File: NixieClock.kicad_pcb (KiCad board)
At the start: 2 copper layers, 164 parts, among them J1 Barrel_Jack, Q1 MPSA42, Q10 MPSA42, Q11 MPSA42, Q12 MPSA42, Q13 KSP92BU, Q14 KSP92BU, Q15 MPSA42, Q16 MPSA42, Q17 MPSA42, Q18 MPSA42, Q19 KSP92BU, Q2 MPSA42, Q20 KSP92BU, Q21 MPSA42, Q22 MPSA42, Q23 KSP92BU, Q24 KSP92BU, Q25 KSP2907A, Q26 IRF644, Q3 MPSA42, Q4 MPSA42, Q5 MPSA42, Q6 MPSA42, Q7 MPSA42, Q8 MPSA42, Q9 MPSA42, SW1 PB400EEQX, SW2 SW_Push, SW3 SW_Push, SW4 SW_Push, U1 L7805, U10 74LS160, U11 74LS160, U12 74LS160, U13 74LS160, U14 74LS160, U15 74HC4060, U16 4028, U17 74LS151, U18 74LS151, U19 74LS151, U2 MC34063AP, U20 4028, U21 74LS151, U3 74LS14, U4 74LS109, U5 74LS10, U6 74LS08, U7 74LS393, U8 74LS20, U9 74LS160, Y1 32.768 kHz - 12.5pF

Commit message: layout started
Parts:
- added ?: , , F.Cu at (223.0, 143.0)
- added ?: , , F.Cu at (146.0, 143.0)
- added C36: 22n, Capacitor_THT:C_Rect_L7.0mm_W2.5mm_P5.00mm, F.Cu at (163.1, 91.2)
- added REF**: MountingHole_3.2mm_M3_Pad, MountingHole:MountingHole_3.2mm_M3_Pad, F.Cu at (105.0, 26.0)
- added REF**: MountingHole_3.2mm_M3_Pad, MountingHole:MountingHole_3.2mm_M3_Pad, F.Cu at (265.0, 26.0)
- C10: value 220u 25V -> 1u 16V; footprint Capacitor_THT:CP_Radial_D8.0mm_P3.80mm -> Capacitor_THT:CP_Radial_D5.0mm_P2.50mm
- C11: value 680p -> 220u 25V; footprint Capacitor_THT:C_Rect_L7.0mm_W4.5mm_P5.00mm -> Capacitor_THT:CP_Radial_D8.0mm_P3.80mm
- C12: value 10n -> 680p; footprint Capacitor_THT:C_Rect_L7.0mm_W2.5mm_P5.00mm -> Capacitor_THT:C_Rect_L7.0mm_W4.5mm_P5.00mm
- C13: value 3u3 250V -> 10n; footprint Capacitor_THT:CP_Radial_D8.0mm_P3.80mm -> Capacitor_THT:C_Rect_L7.0mm_W2.5mm_P5.00mm
- C14: value 100n -> 3u3 250V; footprint Capacitor_THT:C_Rect_L7.0mm_W2.5mm_P5.00mm -> Capacitor_THT:CP_Radial_D8.0mm_P3.80mm
- C33: value 22p -> 100n; footprint Capacitor_THT:C_Disc_D5.1mm_W3.2mm_P5.00mm -> Capacitor_THT:C_Rect_L7.0mm_W2.5mm_P5.00mm
- C35: value 22n -> 22p; footprint Capacitor_THT:C_Rect_L7.0mm_W2.5mm_P5.00mm -> Capacitor_THT:C_Disc_D5.1mm_W3.2mm_P5.00mm
- C9: value 1u 16V -> 100n; footprint Capacitor_THT:CP_Radial_D5.0mm_P2.50mm -> Capacitor_THT:C_Rect_L7.0mm_W2.5mm_P5.00mm
- F1: footprint Fuse:Fuseholder_Cylinder-5x20mm_Schurter_0031_8201_Horizontal_Open -> NixieClock:5x20 fuse
- Q1, Q10, Q11, Q12, Q13, Q14, Q15, Q16, Q17, Q18, Q19, Q2, Q20, Q21, Q22, Q23, Q24, Q25, Q3, Q4, Q5, Q6, Q7, Q8, Q9: footprint Package_TO_SOT_THT:TO-92_Inline -> Package_TO_SOT_THT:TO-92_Inline_Wide
- SW1: footprint Button_Switch_THT:SW_NKK_BB15AH -> NixieClock:PB400EEQX
- moved U9 215.4 mm to (236.3, 49.5), turned to 90 degrees
- moved U5 206.2 mm to (236.3, 36.8), turned to 90 degrees
- moved R53 205.6 mm to (119.9, 83.4)
- moved L1 205.2 mm to (107.2, 84.4), turned to -90 degrees
- moved U2 204.6 mm to (117.4, 79.9), turned to 90 degrees
- moved C9 200.4 mm to (121.5, 41.7), turned to -90 degrees
- moved Q25 200.3 mm to (120.4, 88.9)
- moved D2 200.0 mm to (117.1, 90.3), turned to 90 degrees
- moved C11 196.7 mm to (122.4, 66.2)
- moved C13 195.3 mm to (138.7, 81.9), turned to 90 degrees
- moved U10 194.1 mm to (236.2, 62.2), turned to 90 degrees
- moved U1 193.6 mm to (131.4, 43.4), turned to -90 degrees
- moved C8 192.0 mm to (126.2, 41.7), turned to -90 degrees
- moved Q26 191.2 mm to (115.6, 97.3)
- moved C12 188.5 mm to (129.6, 74.8), turned to -90 degrees
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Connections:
- C10 pad 1: Net-(C10-Pad1) -> +5V
- C13 pad 1: HT -> Net-(C13-Pad1)
- C14 pad 1: +5V -> HT
- C33 pad 1: Net-(C33-Pad1) -> +5V
- C9 pad 1: +5V -> +12V
- R51 pad 2: Net-(C10-Pad1) -> Net-(C11-Pad1)
- R52 pad 2: Net-(C10-Pad1) -> Net-(C11-Pad1)
- R54 pad 2: Net-(C12-Pad1) -> Net-(C13-Pad1)
- R55 pad 1: Net-(C12-Pad1) -> Net-(C13-Pad1)
- R59 pad 1: Net-(C33-Pad1) -> Net-(C34-Pad1)
- R60 pad 2: Net-(C34-Pad1) -> Net-(C35-Pad1)
- R61 pad 2: Net-(C35-Pad1) -> Net-(C36-Pad1)
- U15 pad 9: Net-(C34-Pad1) -> Net-(C35-Pad1)
- U2 pad 3: Net-(C11-Pad1) -> Net-(C12-Pad1)
- U2 pad 5: Net-(C12-Pad1) -> Net-(C13-Pad1)
- U2 pad 6: Net-(C10-Pad1) -> Net-(C11-Pad1)
- U3 pad 5: Net-(C35-Pad1) -> Net-(C36-Pad1)
- Y1 pad 1: Net-(C34-Pad1) -> Net-(C35-Pad1)
- Y1 pad 2: Net-(C33-Pad1) -> Net-(C34-Pad1)
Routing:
- net +5V: track 0.00 -> 659.9 mm
- net GND: track 0.00 -> 274.7 mm
- net HT: track 0.00 -> 206.1 mm
- net 4Hz: track 0.00 -> 180.9 mm
- net K4: track 23.1 -> 200.7 mm
- net K3: track 23.1 -> 198.5 mm
- net K5: track 23.9 -> 196.0 mm
- net K2: track 23.4 -> 193.8 mm
- net K7: track 23.2 -> 192.8 mm
- net K6: track 23.5 -> 192.1 mm
- net K1: track 22.8 -> 190.7 mm
- net K8: track 23.1 -> 185.3 mm
- net KDP: track 0.00 -> 160.5 mm
- net K9: track 22.8 -> 182.9 mm
- net COM: track 0.00 -> 159.8 mm
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- added copper zone on B.Cu, net GND
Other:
- board outline added: 170 x 140 mm

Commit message: Layout completed
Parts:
- added 12V: Symbol_Barrel_Polarity, Symbol:Symbol_Barrel_Polarity, F.Cu at (142.5, 35.3)
- added G***: LOGO, NixieClock:NixieTTL_logo, F.Cu at (187.2, 103.2)
- added REF**: Symbol_Highvoltage_Type1_CopperTop_Small, Symbol:Symbol_Highvoltage_Type1_CopperTop_Small, F.Cu at (162.0, 141.1)
- added REF**: Symbol_Highvoltage_Type1_CopperTop_Small, Symbol:Symbol_Highvoltage_Type1_CopperTop_Small, F.Cu at (209.1, 141.1)
- added REF**: Symbol_HighVoltage_Type2_CopperTop_VerySmall, Symbol:Symbol_HighVoltage_Type2_CopperTop_VerySmall, F.Cu at (115.6, 107.9)
- moved R57 67.9 mm to (248.7, 106.0), turned to 0 degrees
- moved R58 62.2 mm to (248.7, 102.8), turned to 0 degrees
- moved R56 46.6 mm to (248.6, 99.5), turned to 0 degrees
- moved F1 33.8 mm to (138.3, 56.3)
- moved D1 25.5 mm to (130.3, 63.9), turned to 90 degrees
- moved C8 23.9 mm to (114.0, 62.2)
- moved SW1 22.1 mm to (119.8, 46.3)
- moved U1 20.9 mm to (113.9, 55.0), turned to 0 degrees
- moved C9 18.6 mm to (114.0, 58.7), turned to 0 degrees
- moved C11 18.1 mm to (104.4, 64.2)
- moved C13 17.4 mm to (126.0, 69.9), turned to 0 degrees
- moved J1 16.3 mm to (135.8, 42.9)
- moved L1 15.0 mm to (107.0, 99.4), turned to 0 degrees
- moved R50 12.7 mm to (156.4, 37.0), turned to 0 degrees
- moved R53 12.1 mm to (126.1, 73.0), turned to -90 degrees
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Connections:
- net Net-(D3-Pad2) renamed /Power Supply/SMPS_SW
- net Net-(L1-Pad1) renamed /Power Supply/SMPS_IN
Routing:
- net GND: track 274.7 -> 833.0 mm, vias 0 -> 6
- net +5V: track 659.9 -> 827.7 mm
- net Net-(R57-Pad2): track 2.54 -> 111.4 mm, vias 0 -> 3
- net CA3: track 20.9 -> 116.2 mm, vias 0 -> 2
- net CA1: track 34.3 -> 126.2 mm, vias 0 -> 2
- net CA4: track 14.6 -> 102.5 mm, vias 0 -> 1
- net CA0: track 40.0 -> 127.5 mm, vias 0 -> 3
- net CA2: track 28.7 -> 115.2 mm, vias 0 -> 3
- net AN2: track 29.9 -> 110.1 mm, vias 0 -> 4
- net Net-(R58-Pad2): track 2.54 -> 81.9 mm, vias 0 -> 1
- net AN1: track 43.6 -> 121.5 mm, vias 0 -> 3
- net S_UN_A: track 98.5 -> 172.8 mm, vias 0 -> 5
- net AN6: track 0.00 -> 60.8 mm, vias 0 -> 1
- net CA5: track 0.00 -> 59.7 mm
- net CA6: track 0.00 -> 58.7 mm
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- added copper zone on F.Cu, net /Power Supply/SMPS_IN
- added copper zone on F.Cu, net /Power Supply/SMPS_SW
- added copper zone on F.Cu, net HT
- added copper zone on F.Cu, net Net-(C11-Pad1)
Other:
- board size 170 x 140 mm -> 170 x 132 mm
- board text added: "2023"
- board text added: "HOUR"
- board text added: "MIN"
- board text added: "SEC"
- board text added: "Tomás Henriques Pablo Costas"

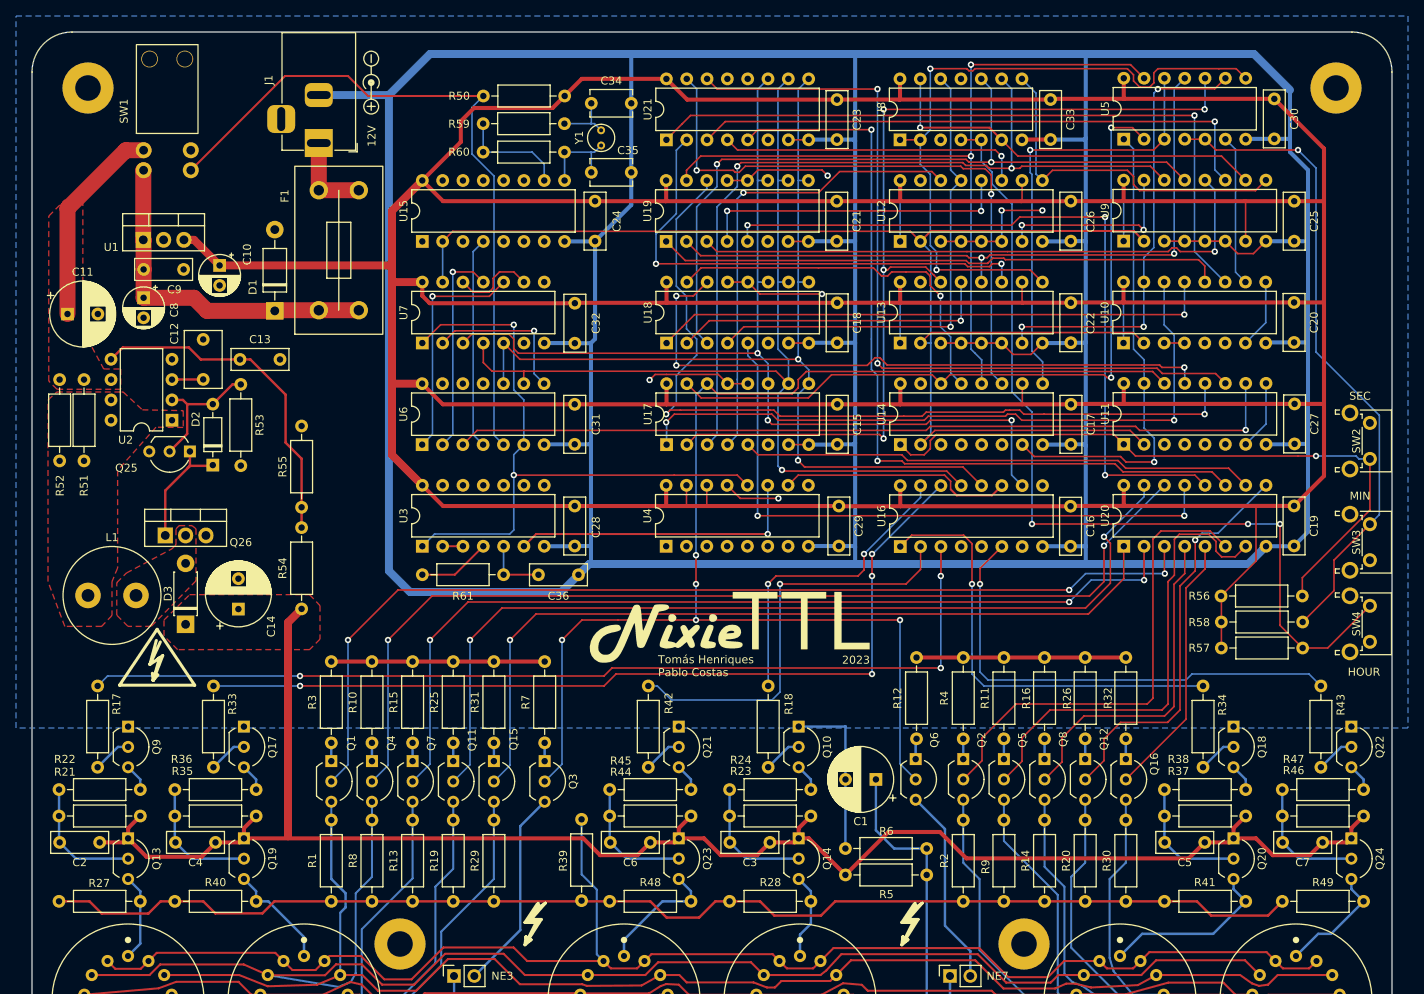
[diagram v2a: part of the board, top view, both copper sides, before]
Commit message: Implemented changes from pablo_cambios branch. Generated Gerbers
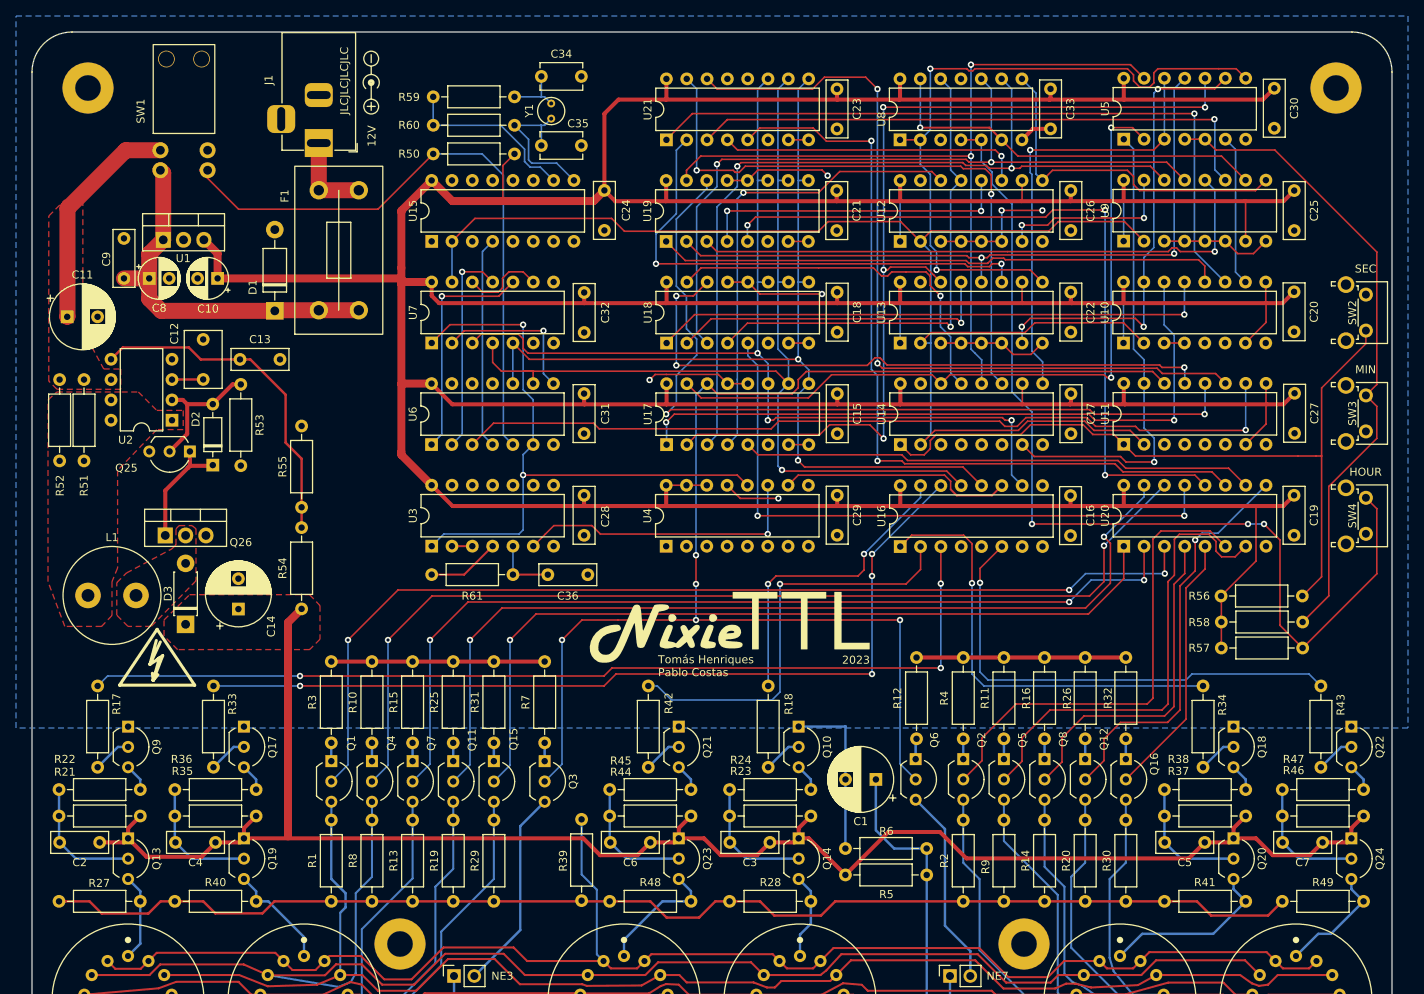
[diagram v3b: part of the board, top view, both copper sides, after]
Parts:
- removed the REF** at (162.0, 141.1)
- removed the REF** at (209.1, 141.1)
- moved SW3 16.1 mm to (266.7, 74.4)
- moved SW2 16.0 mm to (266.7, 61.8)
- moved SW4 13.5 mm to (266.7, 87.2)
- moved R50 9.58 mm to (150.2, 44.2)
- moved C34 7.09 mm to (163.7, 34.6)
- moved C35 7.09 mm to (163.7, 43.2)
- moved R59 7.09 mm to (160.3, 37.1)
- moved R60 7.09 mm to (150.2, 40.7)
- moved Y1 7.09 mm to (164.9, 39.8)
- moved C9 2.70 mm to (111.5, 59.8), turned to 90 degrees
- moved C8 2.52 mm to (114.6, 59.8), turned to 0 degrees
- moved U1 2.49 mm to (116.4, 55.0)
- moved SW1 2.10 mm to (122.0, 46.3)
- moved C24 1.78 mm to (171.6, 48.8)
- moved C28 1.78 mm to (169.0, 86.9)
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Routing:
- net GND: track 833.0 -> 181.2 mm
- net +5V: track 827.7 -> 761.3 mm
- net Net-(R57-Pad2): track 111.4 -> 122.9 mm
- net Net-(R56-Pad2): track 82.8 -> 93.4 mm, vias 1 -> 0
- net DISP_EN: track 88.3 -> 78.1 mm
- net Net-(R59-Pad2): track 13.9 -> 22.4 mm
- net Net-(C35-Pad1): track 11.0 -> 19.3 mm
- net 4Hz: track 180.9 -> 185.1 mm
- net +12V: track 43.6 -> 47.0 mm
- net Net-(C11-Pad1): track 25.7 -> 28.2 mm
- net Net-(U12-Pad7): track 23.8 -> 22.4 mm
- net Net-(U16-Pad10): track 125.0 -> 123.6 mm
- net Net-(U19-Pad5): track 92.4 -> 93.7 mm
- net S_UN_D: track 100.6 -> 101.9 mm
- net Net-(U16-Pad12): track 118.9 -> 117.8 mm
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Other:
- board text added: "JLCJLCJLCJLC"
